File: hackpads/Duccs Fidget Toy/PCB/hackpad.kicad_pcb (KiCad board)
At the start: 2 copper layers, 42 x 61.5 mm, 7 parts, among them SW1 SW_Push, SW2 SW_Push, SW3 SW_Push, SW4 SW_Push, U1 XIAO-RP2040-DIP

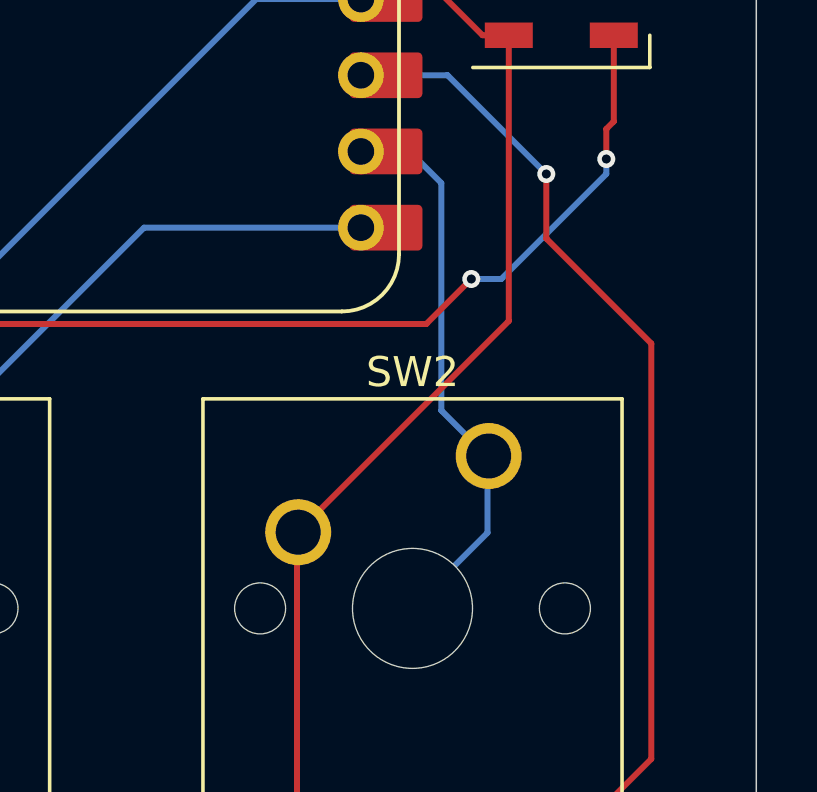
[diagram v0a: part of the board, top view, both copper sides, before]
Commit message: Fix DRC violation
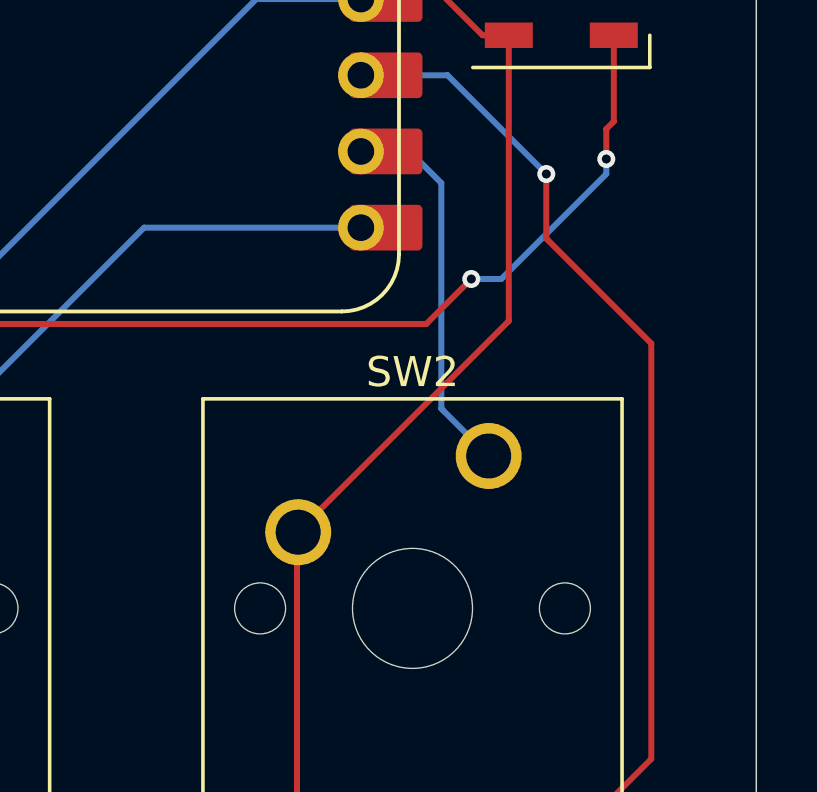
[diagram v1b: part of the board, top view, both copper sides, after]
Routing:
- net Net-(U1-GPIO2/SCK): track 19.0 -> 12.9 mm
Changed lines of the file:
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@@
 	)
 	(segment
-		(start 120 45.3)
-		(end 118.9485 44.2485)
+		(start 120.06 52.88)
+		(end 120 52.82)
+		(width 0.2)
+		(layer "B.Cu")
+		(net 7)
+	)
+	(segment
+		(start 120.06 52.88)
+		(end 121.58 54.4)
+		(width 0.2)
+		(layer "B.Cu")
+		(net 7)
+	)
+	(segment
+		(start 120 52.82)
+		(end 120 45.3)
 		(width 0.2)
 		(layer "B.Cu")
@@
 	)
 	(segment
-		(start 121.54 56.96)
-		(end 121.54 54.42)
+		(start 120 45.3)
+		(end 118.9485 44.2485)
 		(width 0.2)
 		(layer "B.Cu")
-		(net 7)
-	)
-	(segment
-		(start 121.54 54.42)
-		(end 120 52.88)
-		(width 0.2)
-		(layer "B.Cu")
-		(net 7)
-	)
-	(segment
-		(start 120 52.88)
-		(end 120 45.3)
-		(width 0.2)
-		(layer "B.Cu")
-		(net 7)
-	)
-	(segment
-		(start 119 59.5)
-		(end 121.54 56.96)
-		(width 0.2)
-		(layer "B.Cu")
